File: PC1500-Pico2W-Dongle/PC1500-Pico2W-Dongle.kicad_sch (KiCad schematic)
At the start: 65 parts, among them J1 PC1500_60Pin_Connector, J2 microSD, J3 Spare GPIO (GP28), J5 GP2_Spare_IO, Q1 Si2333, Q2 MMBT2222A, U1 Pico2W, U2 AS6C62256-55SIN, U3 SLG46826G, U4 SLG46826G, U5 SC18IS602B, U6 TXS0108EPWR, U7 AP1117-ADJ, U8 TCA9406DC

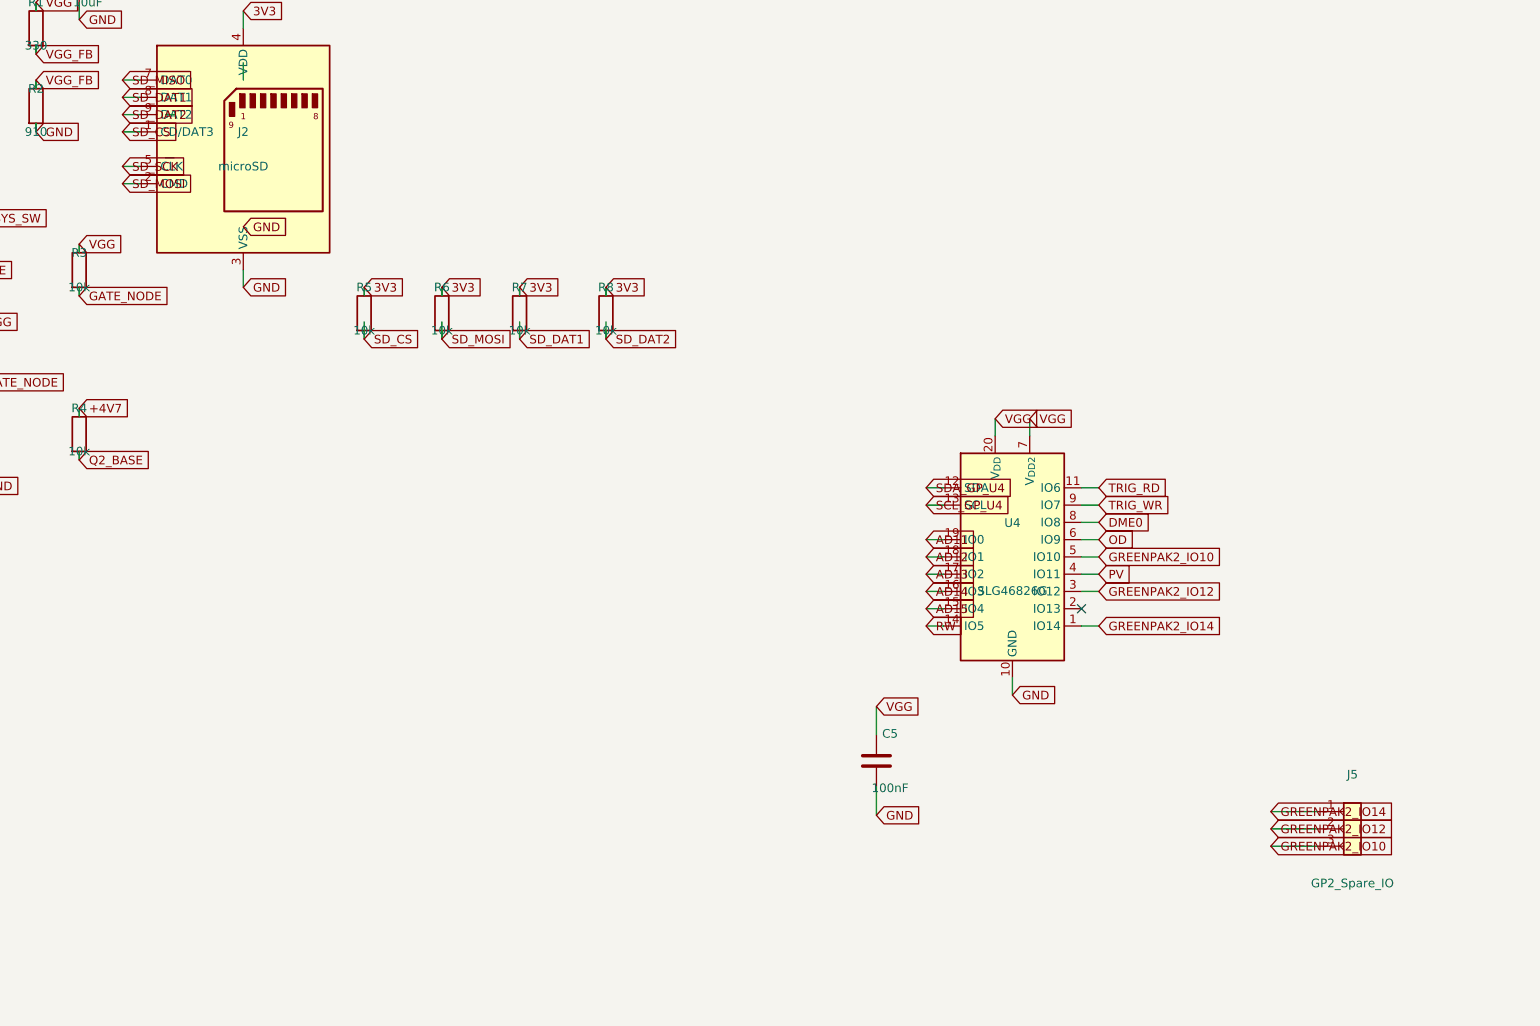
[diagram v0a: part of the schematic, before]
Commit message: Fix microSD pin 6 (GND) and pin 1 (unused, needs pull-up) on all 4 boards
Pin 6 and pin 3 were coincident in the generic SD_Card_Device symbol,
forcing GND onto the same net as CMD/MOSI. Relocated pin 6's local
coordinate and gave it its own wire+label on all four schematics
(RP2350B-BLE and Pico2W-Dongle, each with and without level shifters).

Pin 1 (symbol name CD/DAT3) is unused in this design but needs a 10K
pull-up to 3.3V rather than being left floating, matching the existing
SD_CS/SD_MOSI/SD_DAT1/SD_DAT2 pull-up pattern. Added the missing
wire+label+resistor to the three boards that lacked it
(Pico2W-Dongle-no-level-shifters already had it via R10).

Co-Authored-By: Claude Sonnet 5 <noreply@anthropic.com>
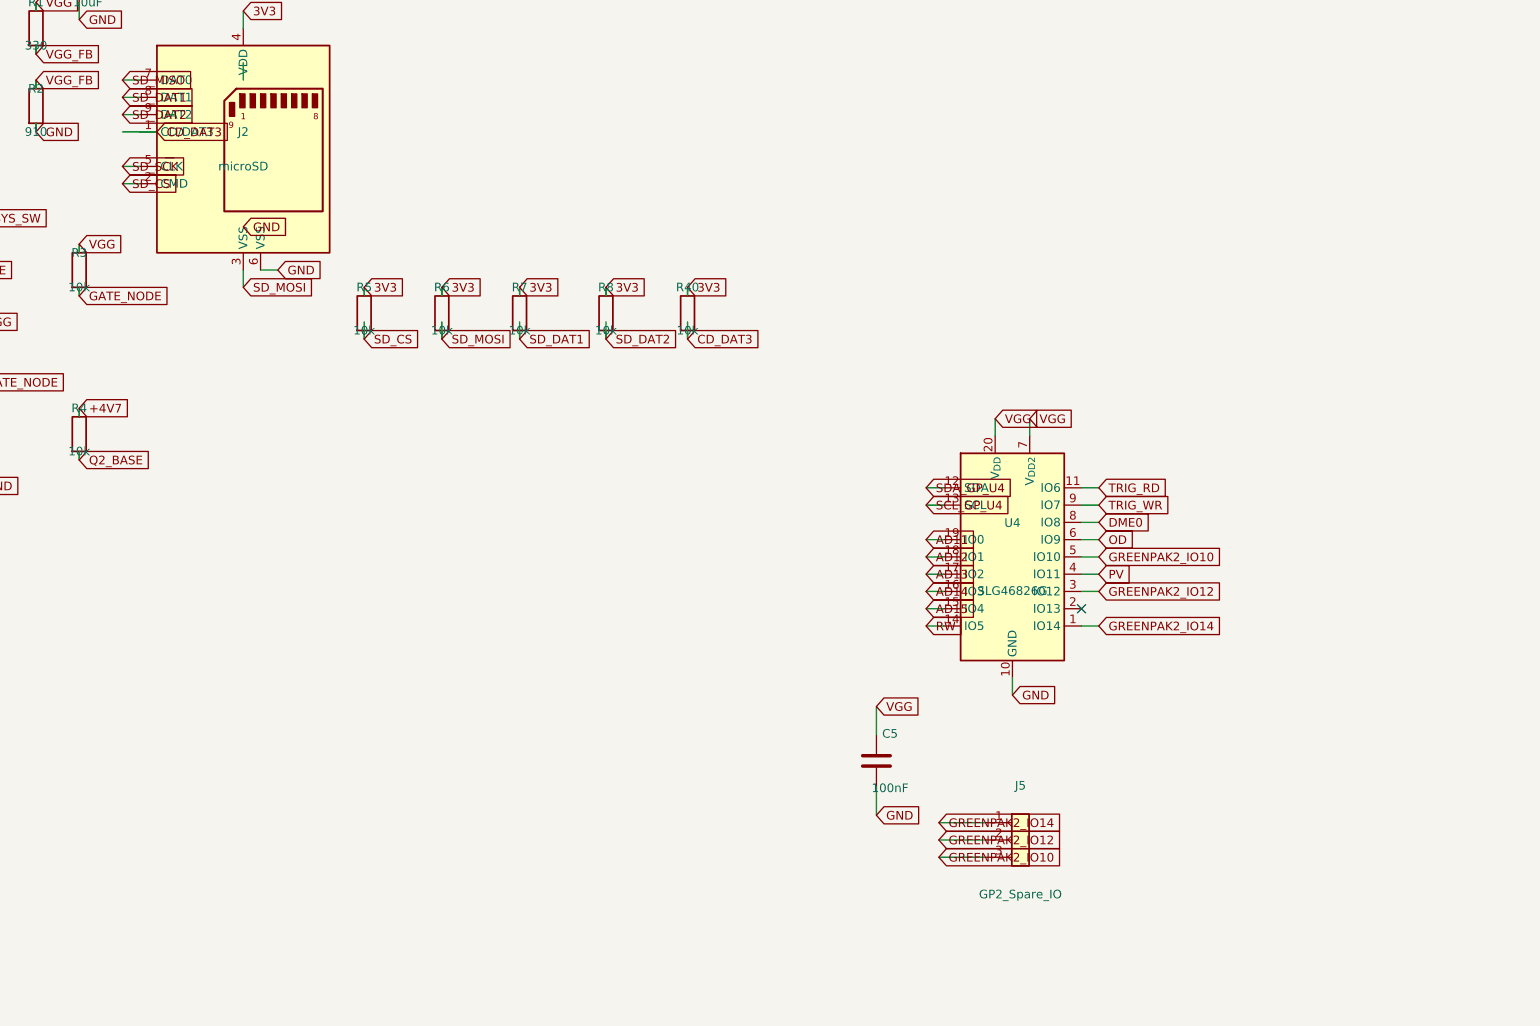
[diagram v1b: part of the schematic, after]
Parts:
- added R40: 10k, Resistor_SMD:R_0201_0603Metric, symbol Device:R
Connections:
- net 3V3: now also R40.1
- net GND: no longer J2.3 (VSS)
- net SD_CS: now also J2.2 (CMD); no longer J2.1 (CD/DAT3)
- net SD_MOSI: now also J2.3 (VSS); no longer J2.2 (CMD)
- new net CD_DAT3: J2.1 (CD/DAT3), R40.2
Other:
- moved on the sheet: J5
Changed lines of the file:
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@@
 	(wire
 		(pts
-			(xy 594.92 337.46) (xy 588 337.46)
+			(xy 546.1 339.09) (xy 539.18 339.09)
 		)
 		(stroke
@@
 	(wire
 		(pts
-			(xy 594.92 340) (xy 588 340)
+			(xy 546.1 341.63) (xy 539.18 341.63)
 		)
 		(stroke
@@
 	(wire
 		(pts
-			(xy 594.92 342.54) (xy 588 342.54)
+			(xy 546.1 344.17) (xy 539.18 344.17)
 		)
 		(stroke
@@
 		)
 	)
+	(wire
+		(pts
+			(xy 439.42 257.81) (xy 441.96 257.81)
+		)
+		(stroke
+			(width 0)
+			(type default)
+		)
+		(uuid "j2gnd0001-a1a1-4000-8000-j2gnd00001")
+	)
+	(global_label "GND"
+		(shape input)
+		(at 441.96 257.81 0)
+		(effects
+			(font
+				(size 1.27 1.27)
+			)
+			(justify left)
+		)
+		(uuid "j2gnd0002-a1a1-4000-8000-j2gnd00002")
+		(property "Intersheetrefs" "${INTERSHEET_REFS}"
+			(at 441.96 257.81 0)
+			(hide yes)
+			(show_name no)
+			(do_not_autoplace no)
+			(effects
+				(font
+					(size 1.27 1.27)
+				)
+			)
+		)
+	)
 	(global_label "AD4_PICO"
 		(shape input)
@@
 	(global_label "SD_CS"
 		(shape input)
-		(at 419.1 237.49 0)
+		(at 419.1 245.11 0)
 		(effects
 			(font
@@
 		)
 		(property "Intersheetrefs" "${INTERSHEET_REFS}"
-			(at 419.1 237.49 0)
+			(at 419.1 245.11 0)
 			(hide yes)
 			(show_name no)
@@
 	(global_label "GREENPAK2_IO14"
 		(shape input)
-		(at 588 337.46 0)
+		(at 539.18 339.09 0)
 		(effects
 			(font
@@
 		)
 		(property "Intersheetrefs" "${INTERSHEET_REFS}"
-			(at 588 337.46 0)
+			(at 539.18 339.09 0)
 			(hide yes)
 			(show_name no)
@@
 	(global_label "GREENPAK2_IO12"
 		(shape input)
-		(at 588 340 0)
+		(at 539.18 341.63 0)
 		(effects
 			(font
@@
 		)
 		(property "Intersheetrefs" "${INTERSHEET_REFS}"
-			(at 588 340 0)
+			(at 539.18 341.63 0)
 			(hide yes)
 			(show_name no)
@@
 	(global_label "GREENPAK2_IO10"
 		(shape input)
-		(at 588 342.54 0)
+		(at 539.18 344.17 0)
 		(effects
 			(font
@@
 		)
 		(property "Intersheetrefs" "${INTERSHEET_REFS}"
-			(at 588 342.54 0)
+			(at 539.18 344.17 0)
 			(hide yes)
 			(show_name no)
@@
 	(global_label "SD_MOSI"
 		(shape input)
-		(at 419.1 245.11 0)
+		(at 436.88 260.35 0)
 		(effects
 			(font
@@
 		)
 		(property "Intersheetrefs" "${INTERSHEET_REFS}"
-			(at 419.1 245.11 0)
+			(at 436.88 260.35 0)
 			(hide yes)
 			(show_name no)
@@
 		)
 	)
-	(global_label "GND"
+	(global_label "SD_DAT2"
 		(shape input)
-		(at 436.88 260.35 0)
+		(at 490.22 267.97 0)
 		(effects
 			(font
@@
 		)
 		(property "Intersheetrefs" "${INTERSHEET_REFS}"
-			(at 436.88 260.35 0)
+			(at 490.22 267.97 0)
 			(hide yes)
 			(show_name no)
@@
 		)
 	)
-	(global_label "SD_DAT2"
+	(wire
+		(pts
+			(xy 421.64 237.49) (xy 424.18 237.49)
+		)
+		(stroke
+			(width 0)
+			(type default)
+		)
+		(uuid "j2pu10001-a1a1-4000-8000-j2pu1000021")
+	)
+	(global_label "CD_DAT3"
 		(shape input)
-		(at 490.22 267.97 0)
+		(at 424.18 237.49 0)
 		(effects
 			(font
@@
 			(justify left)
 		)
+		(uuid "j2pu10002-a1a1-4000-8000-j2pu1000022")
 		(property "Intersheetrefs" "${INTERSHEET_REFS}"
-			(at 490.22 267.97 0)
+			(at 424.18 237.49 0)
+			(hide yes)
+			(show_name no)
+			(do_not_autoplace no)
+			(effects
+				(font
+					(size 1.27 1.27)
+				)
+			)
+		)
+	)
+	(wire
+		(pts
+			(xy 502.22 265.43) (xy 502.22 267.97)
+		)
+		(stroke
+			(width 0)
+			(type default)
+		)
+		(uuid "j2pu10003-a1a1-4000-8000-j2pu1000023")
+	)
+	(global_label "CD_DAT3"
+		(shape input)
+		(at 502.22 267.97 0)
+		(effects
+			(font
+				(size 1.27 1.27)
+			)
+			(justify left)
+		)
+		(uuid "j2pu10004-a1a1-4000-8000-j2pu1000024")
+		(property "Intersheetrefs" "${INTERSHEET_REFS}"
+			(at 502.22 267.97 0)
+			(hide yes)
+			(show_name no)
+			(do_not_autoplace no)
+			(effects
+				(font
+					(size 1.27 1.27)
+				)
+			)
+		)
+	)
+	(wire
+		(pts
+			(xy 502.22 261.62) (xy 502.22 260.35)
+		)
+		(stroke
+			(width 0)
+			(type default)
+		)
+		(uuid "j2pu10005-a1a1-4000-8000-j2pu1000025")
+	)
+	(global_label "3V3"
+		(shape input)
+		(at 502.22 260.35 0)
+		(effects
+			(font
+				(size 1.27 1.27)
+			)
+			(justify left)
+		)
+		(uuid "j2pu10006-a1a1-4000-8000-j2pu1000026")
+		(property "Intersheetrefs" "${INTERSHEET_REFS}"
+			(at 502.22 260.35 0)
 			(hide yes)
 			(show_name no)
@@
 	(symbol
 		(lib_id "Connector_Generic:Conn_01x03")
-		(at 600 340 0)
+		(at 551.18 341.63 0)
 		(unit 1)
 		(body_style 1)
@@
 		(dnp no)
 		(property "Reference" "J5"
-			(at 600 332 0)
+			(at 551.18 333.63 0)
 			(show_name no)
 			(do_not_autoplace no)
@@
 		)
 		(property "Value" "GP2_Spare_IO"
-			(at 600 348 0)
+			(at 551.18 349.63 0)
 			(show_name no)
 			(do_not_autoplace no)
@@
 		)
 		(property "Footprint" "Connector_PinHeader_2.54mm:PinHeader_1x03_P2.54mm_Vertical"
-			(at 600 340 0)
+			(at 551.18 341.63 0)
 			(hide yes)
 			(show_name no)
@@
 		)
 		(property "Datasheet" ""
-			(at 600 340 0)
+			(at 551.18 341.63 0)
 			(show_name no)
 			(do_not_autoplace no)
@@
 		)
 		(property "Description" ""
-			(at 600 340 0)
+			(at 551.18 341.63 0)
 			(show_name no)
 			(do_not_autoplace no)
@@
 					(unit 1)
 				)
+			)
+		)
+	)
+	(symbol
+		(lib_id "Device:R")
+		(at 502.22 264.16 0)
+		(unit 1)
+		(body_style 1)
+		(exclude_from_sim no)
+		(in_bom yes)
+		(on_board yes)
+		(in_pos_files yes)
+		(dnp no)
+		(uuid "j2pu1r40-a1a1-4000-8000-j2pu1r40031")
+		(property "Reference" "R40"
+			(at 502.22 260.35 0)
+			(show_name no)
+			(do_not_autoplace no)
+			(effects
+				(font
+					(size 1.27 1.27)
+				)
+			)
+		)
+		(property "Value" "10k"
+			(at 502.22 266.7 0)
+			(show_name no)
+			(do_not_autoplace no)
+			(effects
+				(font
+					(size 1.27 1.27)
+				)
+			)
+		)
+		(property "Footprint" "Resistor_SMD:R_0201_0603Metric"
+			(at 502.22 264.16 0)
+			(hide yes)
+			(show_name no)
+			(do_not_autoplace no)
+			(effects
+				(font
+					(size 1.27 1.27)
+				)
+			)
+		)
+		(property "Datasheet" ""
+			(at 502.22 264.16 0)
+			(show_name no)
+			(do_not_autoplace no)
+			(effects
+				(font
+					(size 1.27 1.27)
+				)
+			)
+		)
+		(property "Description" ""
+			(at 502.22 264.16 0)
+			(show_name no)
+			(do_not_autoplace no)
+			(effects
+				(font
+					(size 1.27 1.27)
+				)
+			)
+		)
+		(pin "1"
+			(uuid "j2pu1r40-a1a1-4000-8000-j2pu1r40032")
+		)
+		(pin "2"
+			(uuid "j2pu1r40-a1a1-4000-8000-j2pu1r40033")
+		)
+		(instances
+			(project "PC1500-Pico2W-Dongle"
+				(path "/4877a8cd-59b3-4d48-abe6-7a71a73105ef"
+					(reference "R40")
+					(unit 1)
+				)

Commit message: Swap discontinued AP1117-ADJ for NCP1117-ADJ, clean up part names for BOM/CPL
AP1117-ADJ (U7, both Pico2W-Dongle variants) is discontinued; KiCad's own
library even flags it obsolete. Swapped to NCP1117-ADJ_SOT223, a
pin-compatible drop-in (same SOT-223 footprint, same graphics via the
library's "extends" relationship) - no rewiring needed. Had to embed the
new symbol into each schematic's symbol cache too, since just changing
the instance lib_id left it unresolvable and silently dropped from the
netlist/BOM.

Replaced dashes and underscores with spaces in all instance-level part
Values across both dongle boards, and in the no-level-shifters board's
exported BOM Footprint column and resistor values (added the missing
Ohm symbol) - all for cleaner JLCPCB/distributor part matching.

Co-Authored-By: Claude Sonnet 5 <noreply@anthropic.com>
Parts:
- J1: value PC1500_60Pin_Connector -> PC1500 60Pin Connector
- J5: value GP2_Spare_IO -> GP2 Spare IO
- JP1, JP2: value GP1-GP2 I2C link -> GP1 GP2 I2C link
- Jumper1: value Jumper_2_Bridged -> Jumper 2 Bridged
- U2: value AS6C62256-55SIN -> AS6C62256 55SIN
- U7: value AP1117-ADJ -> NCP1117 ADJ; symbol Regulator_Linear:AP1117-ADJ -> Regulator_Linear:NCP1117-ADJ_SOT223
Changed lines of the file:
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@@
 	)
 	(symbol
-		(lib_id "Regulator_Linear:AP1117-ADJ")
+		(lib_id "Regulator_Linear:NCP1117-ADJ_SOT223")
 		(at 394.97 204.47 0)
 		(unit 1)
@@
 			)
 		)
-		(property "Value" "AP1117-ADJ"
+		(property "Value" "NCP1117 ADJ"
 			(at 394.97 207.01 0)
 			(show_name no)
@@
 			)
 		)
-		(property "Value" "PWR_FLAG"
+		(property "Value" "PWR FLAG"
 			(at 140 255 0)
 			(show_name no)
@@
 			)
 		)
-		(property "Value" "Jumper_2_Bridged"
+		(property "Value" "Jumper 2 Bridged"
 			(at 500 55 0)
 			(show_name no)
@@
 			)
 		)
-		(property "Value" "PWR_FLAG"
+		(property "Value" "PWR FLAG"
 			(at 100 255 0)
 			(show_name no)
@@
 			)
 		)
-		(property "Value" "AS6C62256-55SIN"
+		(property "Value" "AS6C62256 55SIN"
 			(at 400 155 0)
 			(show_name no)
@@
 			)
 		)
-		(property "Value" "GP2_Spare_IO"
+		(property "Value" "GP2 Spare IO"
 			(at 551.18 349.63 0)
 			(show_name no)
@@
 			)
 		)
-		(property "Value" "GP1-GP2 I2C link"
+		(property "Value" "GP1 GP2 I2C link"
 			(at 550 404.92 0)
 			(show_name no)
@@
 			)
 		)
-		(property "Value" "PC1500_60Pin_Connector"
+		(property "Value" "PC1500 60Pin Connector"
 			(at 50 155 0)
 			(show_name no)
@@
 			)
 		)
-		(property "Value" "GP1-GP2 I2C link"
+		(property "Value" "GP1 GP2 I2C link"
 			(at 550 394.92 0)
 			(show_name no)
@@
 			)
 		)
-		(property "Value" "PWR_FLAG"
+		(property "Value" "PWR FLAG"
 			(at 120 255 0)
 			(show_name no)
